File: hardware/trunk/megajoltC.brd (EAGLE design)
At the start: 79.9 x 63 mm, 92 parts, among them IC2 MCP1826, IC9 74AC240, U3 MAX9924, U4 ZXMS6004FF, U5 MAX9924, U6 ZXMS6004FF, U7 MCP1700, U8 FAN8303, X1 MINI_USB_SHIELD, X2 MOLEX_MINIFIT-22

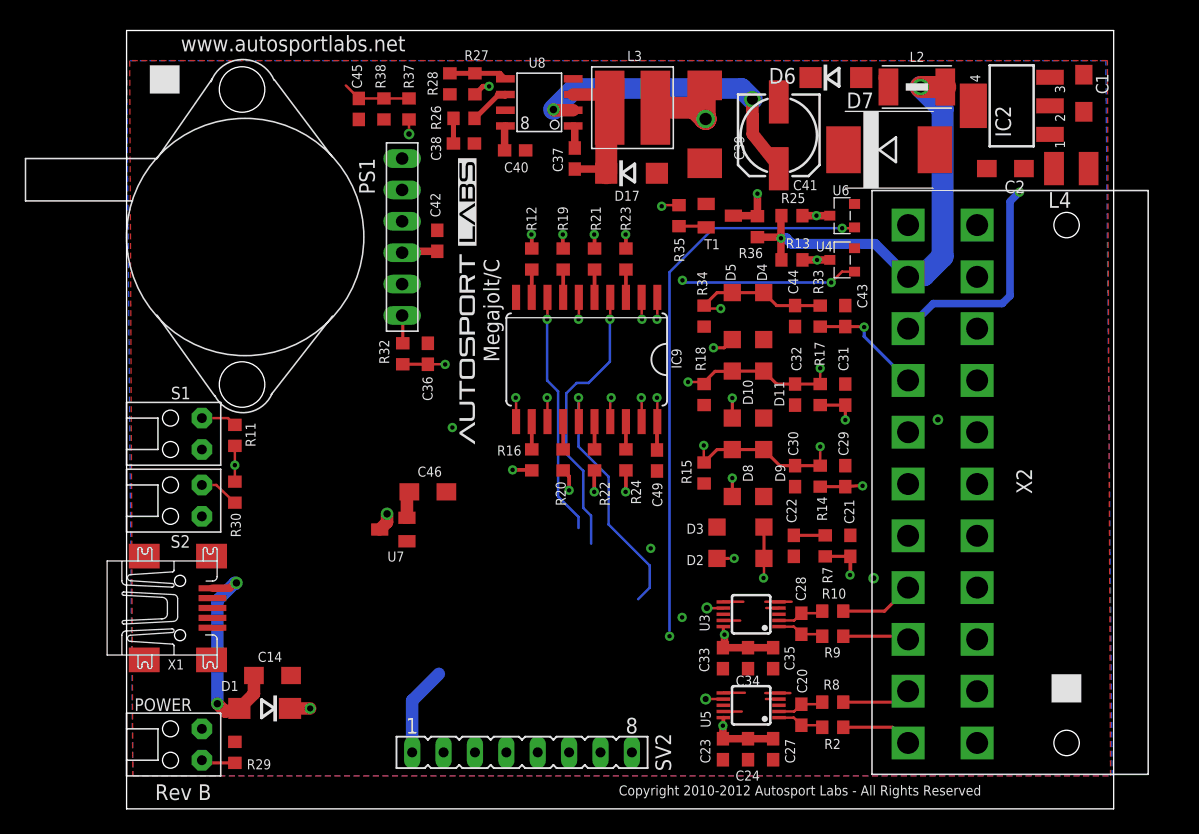
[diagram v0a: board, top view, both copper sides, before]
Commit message: Schematic V1 for MJ2/C
Also added pinmux for xmc4200.  Board is partially routed to assist in pinout
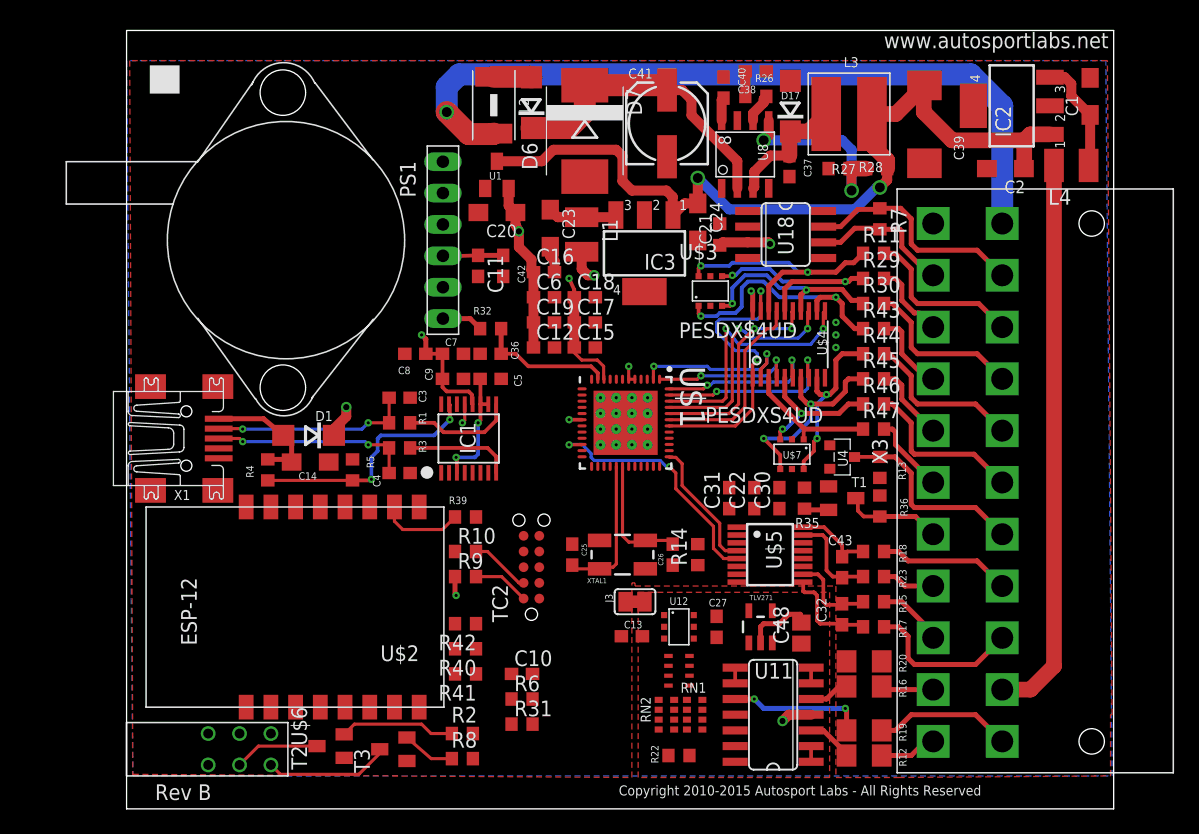
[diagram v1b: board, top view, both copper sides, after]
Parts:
- removed C28: 1nF, rcl:C0603
- removed C29: .001uf, rcl:C0603
- removed C33: 10nF, rcl:C0603
- removed C34: 0.1uF, rcl:C0603
- removed C35: 1uF, rcl:C0603
- removed C44: 0.22uf, rcl:C0603
- removed C45: .1uf, rcl:C0603
- removed C46: 10uF, rcl:SMC_A
- removed C49: 0.1uf, rcl:C0603
- removed D10, D11, D2, D3, D4, D5, D8, D9: schottky, smt_diodes:SOD123
- removed IC9: 74AC240, 74xx-eu:SO20W
- removed POWER, S1, S2: PANEL_LED, LEDs:RIGHTANGLE_CML_5323F5
- removed R21, R24, R25: 1K, rcl:R0603
- removed R33: 20K 1%, rcl:R0603
- removed R34: 39K 1%, rcl:R0603
- removed R37: 51K 1%, rcl:R0603
- removed R38: 10K 1%, rcl:R0603
- removed SV2: (no value), con-lsta:FE08
- removed U3, U5: MAX9924, max9924_9927:UMAX10
- removed U6: ZXMS6004FF, power_mosfets:SOT-23
- removed U7: MCP1700, mcp1700:SOT-23
- removed X2: MOLEX_MINIFIT-22, molex_mini-fit:MOLEX_MINIFIT-22
- added C10, C12: 10uF, resistor:C0603
- added C11: 0.1uf, rcl:C0603
- added C13, C15, C16, C17, C18, C19, C7, C8: 100nF, resistor:C0603
- added C25, C26: 33pF, SparkFun:0603
- added C3, C4: 47pF, resistor:C0603
- added C48: 0.1uF, rcl:C0805
- added C5: 100nf, resistor:C0603
- added C6, C9: 4.7uF, resistor:C0603
- added CN2: (no value), cap_array:1206_ARRAY
- added IC1: IC_FT230X-SSOP-16, dp_devices:SSOP-16-FTDI
- added IC3: MCP1826, linear:SOT223
- added J3: JUMPER_CLOSEDTHICK, jumpers:JUMPER_CLOSED_THICK
- added L1: 1uH, smt_inductors:1210
- added R1, R3: 27, resistor:R0603
- added R31: 100, resistor:R0603
- added R39: 1k, resistor:R0603
- added R4: 4.7k, resistor:R0603
- added R40, R41, R42: 100, rcl:R0603
- added R43, R44, R45, R46, R47: 1K, rcl:R0603
- added R5, R6: 10k, resistor:R0603
- added RN1: 5.6K, resistor-dil:0603-ARC
- added RN2: 10K, resistor-dil:0603-ARC
- added T2, T3: (no value), transistor:SOT23-EBC
- added TC2: TC2050-IDC-NL, TagConnect:TC2050-IDC-NL
- added TLV271: TLV271, texas_instruments:SOT23-5
- added U$1: INF-PG-VQFN-48-53-5200X5200TE5, infineon_xmc:INF-PG-VQFN-48-53-5200X5200TE5PRIMARY
- added U$2: ESP8266_ESP-12, ESP8266-ESP12:ESP8266-ESP12
- added U$3, U$7, U12: PESDXS4UD, smt_diodes:SC-74
- added U$4: 74AC240, dp_devices:TSSOP-20
- added U$5: MAX9926, max9924_9927:QSOP16
- added U$6: TRIPLE_PANEL_LED, LEDs:RIGHT_ANGLE_3_LEDS_DEEP
- added U1: MCP1700, mcp1700:SOT-23
- added U11: TLV274, op_amps:SO14
- added U18: MCP2551SO8, can:SO08
- added X3: MOLEX_MINIFIT-22, molex_mini-fit:MOLEX_MINIFIT-22
- added XTAL1: 8MHz, SparkFun2:CRYSTAL-SMD-5X3
- C20: value 1nF -> 10uF; device rcl:C0603 -> rcl:SMC_A
- C21: value .001uF -> 0.1uF; device rcl:C0603 -> rcl:C0603K
- C22: value 0.22uF -> 10nF
- C23: value 10nF -> 10uF; device rcl:C0603 -> rcl:SMC_A
- C24: value 0.1uF -> 10uF; device rcl:C0603 -> rcl:SMC_A
- C27: value 1uF -> .1uf; device rcl:C0603 -> resistor:C0603
- C30: value 0.22uf -> 0.1uF
- C31: value .001uf -> 1uF
- C32: value 0.22uf -> 1nF
- C43: value .001uf -> 1nF
- R10, R9: value 10K -> 100k; device rcl:R0603 -> resistor:R0603
- R11, R29, R30: value 100 -> 1K
- R12, R16, R19, R20: value 1K -> 10K; device rcl:R0603 -> rcl:R1206
- R14, R17: value 20K 1% -> 10K
- R15, R18: value 39K 1% -> 10K
- R22: value 1K -> 2.1k; device rcl:R0603 -> resistor:R0603
- R23: value 1K -> 10K
- R27: value 18K 1% -> 24K 1%
- R28: value 2.43K 1% -> 2.94K 1%
- R7: value 2.2K -> 120
- moved R29 64.4 mm to (60.5, 42.9), turned to 0 degrees
- moved R30 53.9 mm to (60.5, 40.9), turned to 0 degrees
- moved R11 53.7 mm to (60.5, 45.0), turned to 0 degrees
- moved R12 48.3 mm to (59.7, 4.32), turned to 0 degrees
- moved C20 47.5 mm to (30.0, 48.3), turned to 180 degrees
- moved R19 45.3 mm to (59.7, 6.35), turned to 0 degrees
- moved C23 44.4 mm to (34.3, 47.0)
- moved C24 42.9 mm to (46.2, 47.5)
- moved L2 34.3 mm to (29.7, 56.9), turned to 270 degrees
- moved R27 33.2 mm to (60.7, 51.8), turned to 180 degrees
- moved R23 32.6 mm to (60.5, 18.8), turned to 0 degrees
- moved R16 32.6 mm to (59.7, 9.91), turned to 0 degrees
- moved R28 32.2 mm to (57.7, 51.8), turned to 180 degrees
- moved R8 30.3 mm to (27.2, 4.06)
- moved R10 30.1 mm to (27.4, 20.8)
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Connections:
- removed net +12V: L2.2, R13.2, R25.2, R36.2, X2.P2
- removed net +6V: C2.+, IC2.1
- removed net ADC0: C45.1, R37.2, R38.1
- removed net ADC4: C30.1, D8.A, D9.C, R14.2, R15.2
- removed net ADC5: C32.1, D10.A, D11.C, R17.2, R18.2
- removed net ADC6: C36.1, R32.2
- removed net ADC7: C44.1, D4.C, D5.A, R33.2, R34.2
- removed net AUX_IN: C29.1, R14.1, X2.P6
- removed net GPI0: D2.A, D3.C
- removed net GPO0: IC9.11
- removed net GPO1: IC9.8
- removed net GPO10: IC9.1, IC9.19
- removed net GPO11: U4.1
- removed net GPO2: IC9.13
- removed net GPO3: IC9.6
- removed net GPO4: IC9.15
- removed net GPO5: IC9.4
- removed net GPO6: IC9.17
- removed net GPO7: IC9.2
- removed net GPO8: R35.1
- removed net GPO9: U6.1
- removed net N$14: C20.2, R8.1, U5.2
- removed net N$19: R11.2, S1.A
- removed net N$6: C28.2, R10.1, U3.2
- removed net OPTION_IN: C21.1, R7.1, X2.P7
- removed net PROC_PULSE_IN: C22.1, R7.2
- removed net RESET: SV2.2
- removed net SAFE12V: C41.+, D6.C, D7.C, R37.1, U8.2
- removed net SHIFT_LIGHT: R25.1, U6.3, X2.P20
- removed net TCK: SV2.5
- removed net TDI: SV2.3
- removed net TDO: SV2.6
- removed net TEMP_IN: C43.1, R33.1, X2.P4
- removed net TIMER0: U5.7
- removed net TIMER1: U3.7
- removed net TMS: SV2.4
- removed net V+: C46.+, SV2.1, U7.2
- new net +3V3: C12.1, C13.1, C15.1, C16.1, C17.1, C18.1, C19.1, C20.+, C6.1, C7.1, C8.1, C9.1, IC1.12, R31.2, R6.2, R9.1, TC2.1, U$1.10, U$1.18, U$1.28, U$1.31, U$1.41, U$1.5, U$1.6, U$2.16, U1.2
- new net AGND: C13.2, C27.2, C48.2, CN2.1, CN2.2, CN2.4, J3.1, R22.1, RN2.1, RN2.2, RN2.3, TLV271.2, U$1.17, U11.11, U12.2, U12.5
- new net ANALOG-FREQ_1_OPAMP_OUT1: RN1.6, U11.1, U11.2
- new net ANALOG-FREQ_1_OPAMP_OUT2: RN1.7, U11.6, U11.7
- new net ANALOG-FREQ_1_OPAMP_OUT3: RN1.8, U11.8, U11.9
- new net ANALOG-FREQ_1_OPAMP_OUT4: RN1.4, TLV271.1, TLV271.4
- new net CAM_TIM_IN: U$1.22, U$5.5
- new net CANH: R7.1, U18.7, X3.P21
- new net CANL: R7.2, U18.6, X3.P2
- new net CAN_RX: U$1.15, U18.4
- new net CAN_TX: U$1.26, U18.1
- new net CLT_ADC: RN1.3, RN2.6, U$1.16
- new net CLT_IN: R12.2, X3.P11
- new net CRANK_TIM_IN: U$1.37, U$5.4
- new net ESP_GPIO0: U$2.4
- new net ESP_RXD: U$1.21, U$2.7
- new net ESP_TXD: U$1.24, U$2.8
- new net FTDI_DM: C3.1, R1.1, X1.2
- new net FTDI_DP: C4.1, R3.1, X1.3
- new net FTDI_RXD: IC1.4, U$1.35
- new net FTDI_TXD: IC1.1, U$1.36
- new net FTDI_VBUS_SENSE: IC1.15, R4.1, R5.2
- new net GPO_COIL1: U$1.2, U$4.2
- new net GPO_COIL2: U$1.1, U$4.4
- new net GPO_COIL3: U$1.48, U$4.6
- new net GPO_COIL4: U$1.47, U$4.8
- new net GPO_COIL5: U$1.46, U$4.11
- new net GPO_COIL6: U$1.45, U$4.13
- new net GPO_COIL7: U$1.44, U$4.15
- new net GPO_COIL8: U$1.43, U$4.17
- new net GPO_COIL_EN: U$1.42, U$4.1, U$4.19
- new net IAT_ADC: RN1.1, RN2.8, U$1.14
- new net IAT_IN: R19.2, X3.P12
- new net MAP_ADC: C36.1, R32.2, U$1.11
- new net MAX_DIRN: R14.1, U$5.12
- new net N$1: IC1.8, R3.2
- new net N$17: C10.1, R6.1, U$2.9
- new net N$18: R31.1, U$2.11
- new net N$20: R40.2, U$6.1
- new net N$23: R42.2, U$6.5
- new net N$24: R39.2, U$2.2
- new net N$25: C25.2, U$1.29, XTAL1.3
- new net N$36: R11.1, U$3.6, U$4.18
- new net N$37: R29.1, U$3.4, U$4.16
- new net N$38: R30.1, U$3.3, U$4.14
- new net N$39: R43.1, U$3.1, U$4.12
- new net N$4: C5.1, IC1.10, IC1.11, IC1.3
- new net N$40: R44.1, U$4.9, U$7.6
- new net N$41: R45.1, U$4.7, U$7.4
- new net N$42: R46.1, U$4.5, U$7.3
- new net N$43: R47.1, U$4.3, U$7.1
- new net N$56: C23.+, IC3.3, L1.1
- new net PGM_GPO: U$1.23, U4.1
- new net RAW_+12V: L2.2, X3.P22
- new net SAFE_+12V: C27.1, C41.+, D6.C, D7.C, R13.2, R20.2, R36.2, TLV271.5, U8.2
- new net STATUS_LED_1: R2.2, U$1.20
- new net STATUS_LED_2: R8.2, U$1.19
- new net SWCLK: R10.2, TC2.4, U$1.34
- new net SWDIO: R9.2, TC2.2, U$1.33
- new net TACH_GPO: R35.1, U$1.25
- new net TPS_ADC: RN1.2, RN2.7, U$1.13
- new net VBATT_ADC: R22.2, RN1.5, U$1.12
- new net VDD: C2.+, C24.+, C39.+, IC2.1, IC3.1, L3.P$1, R27.1, U1.3
- new net XMC_RESET: TC2.10, U$1.32
- net +5V: now also C11.1, C21.1, C22.1, C30.1, C31.1, L1.2, R14.2, R40.1, R41.1, R42.1, U$4.20, U$5.14, U11.4, U18.3; no longer C23.1, C24.1, C27.1, C33.1, C34.1, C35.1, C39.+, C49.1, D10.C, D2.C, D5.C, D8.C, IC9.20, L3.P$1, R11.1, R27.1, R30.1, U3.10, U5.10, U7.3
- net CAM_VRS+: now also R17.2, X3.P14; no longer R9.2, X2.P9
- net CAM_VRS-: now also R15.2, X3.P9; no longer R10.2, X2.P8
- net COIL1: now also R11.2, X3.P20; no longer R12.2, X2.P12
- net COIL2: now also R29.2, X3.P3; no longer R16.2, X2.P13
- net COIL3: now also R30.2, X3.P19; no longer R19.2, X2.P14
- net COIL4: now also R43.2, X3.P4; no longer R20.2, X2.P15
- net COIL5: now also R44.2, X3.P18; no longer R21.2, X2.P16
- net COIL6: now also R45.2, X3.P5; no longer R22.2, X2.P17
- net COIL7: now also R46.2, X3.P17; no longer R23.2, X2.P18
- net COIL8: now also R47.2, X3.P6; no longer R24.2, X2.P19
- net CRANK_VRS+: now also R18.2, X3.P15; no longer R2.2, X2.P11
- net CRANK_VRS-: now also R23.2, X3.P8; no longer R8.2, X2.P10
- net GND: now also C10.2, C11.2, C12.2, C15.2, C16.2, C17.2, C18.2, C19.2, C20.-, C23.-, C24.-, C25.1, C26.1, C3.2, C4.2, C5.2, C6.2, C7.2, C8.2, C9.2, IC1.13, IC1.5, IC3.2, IC3.4, J3.2, R10.1, R39.1, R5.1, T2.E, T3.E, TC2.3, U$1.27, U$1.49, U$2.1, U$3.2, U$3.5, U$4.10, U$5.1, U$5.11, U$5.13, U$5.3, U$5.6, U$5.8, U$6.2, U$7.2, U$7.5, U1.1, U18.2, U18.8, X3.P1; no longer C23.2, C24.2, C27.2, C29.2, C32.2, C33.2, C34.2, C35.2, C43.2, C44.2, C45.2, C46.-, C49.2, D11.A, D3.A, D4.A, D9.A, IC9.10, R15.1, R18.1, R29.2, R34.1, R38.2, SV2.7, SV2.8, U3.4, U3.5, U3.6, U3.9, U5.4, U5.5, U5.6, U5.9, U6.2, U7.1, X2.P1
- net N$2: now also T2.B; no longer C20.1, U5.1
- net N$21: now also C26.2, U$1.30, XTAL1.1; no longer R30.2, S2.A
- net N$22: now also R41.2, U$6.3; no longer POWER.C, R29.1
- net N$26: now also CN2.7, U11.3, U12.1; no longer IC9.9
- net N$27: now also C43.1, R18.1, U$5.16; no longer IC9.12, R16.1
- net N$28: now also CN2.8, R16.1, U11.5, U12.6; no longer IC9.7, R19.1
- net N$29: now also C32.1, R15.1, U$5.10; no longer IC9.14, R20.1
- net N$3: now also IC1.9, R1.2; no longer X1.3
- net N$30: now also CN2.5, R19.1, U11.10, U12.4; no longer IC9.5, R21.1
- net N$31: now also C48.1, R20.1, TLV271.3, U12.3; no longer IC9.16, R22.1
- net N$32: now also C32.2, R17.1, U$5.9; no longer IC9.3, R23.1
- net N$33: now also C43.2, R23.1, U$5.15; no longer IC9.18, R24.1
- net N$5: now also R8.1, T3.B; no longer C28.1, R9.1, U3.1
- net PGM_OUT: now also X3.P16; no longer X2.P21
- net PROC_STATUS_LED_OUT1: now also T2.C, U$6.4; no longer S1.C
- net PROC_STATUS_LED_OUT2: now also T3.C, U$6.6; no longer S2.C
- net TACH_OUT: now also X3.P7; no longer X2.P22
- net TPS_IN: now also R16.2, X3.P10; no longer C31.1, R17.1, X2.P5
- net VBUS: now also R4.2
- net VREF: now also X3.P13; no longer X2.P3
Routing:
- net VDD: track 0.00 -> 67.6 mm, vias 0 -> 2
- net COIL1: track 78.4 -> 13.4 mm, vias 1 -> 0
- net RAW_+12V: track 0.00 -> 62.5 mm, vias 0 -> 1
- net COIL3: track 68.4 -> 13.3 mm, vias 1 -> 0
- net TDI: track 49.1 -> 0.00 mm
- net COIL2: track 54.8 -> 6.35 mm, vias 3 -> 0
- net GPO9: track 48.4 -> 0.00 mm, vias 2 -> 0
- net ADC7: track 41.3 -> 0.00 mm, vias 1 -> 0
- net GPO11: track 41.0 -> 0.00 mm, vias 2 -> 0
- net SAFE12V: track 38.7 -> 0.00 mm, vias 3 -> 0
- net GPO8: track 38.5 -> 0.00 mm, vias 1 -> 0
- net ADC5: track 38.0 -> 0.00 mm, vias 3 -> 0
- net +12V: track 37.8 -> 0.00 mm, vias 2 -> 0
- net GPO10: track 37.8 -> 0.00 mm, vias 2 -> 0
- net +3V3: track 0.00 -> 36.9 mm, vias 0 -> 6
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- added copper zone on layer 15, net +3V3
- added copper zone on layer 1, net AGND
- added copper zone on layer 2, net GND
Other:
- board text added: "Copyright 2010-2015 Autosport Labs - All Rights Reserved"
- board text removed: "Copyright 2010-2012 Autosport Labs - All Rights Reserved"

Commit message: Schematic, second draft complete
Also added gitignore
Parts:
- removed C27: .1uf, resistor:C0603
- removed C48: 0.1uF, rcl:C0805
- removed L4: 1uH, smt_inductors:1210
- removed R20: 10K, rcl:R1206
- removed R22: 2.1k, resistor:R0603
- removed T2, T3: (no value), transistor:SOT23-EBC
- removed TLV271: TLV271, texas_instruments:SOT23-5
- removed X3: MOLEX_MINIFIT-22, molex_mini-fit:MOLEX_MINIFIT-22
- added C28: .1uf, resistor:C0603
- added C45: .1uf, rcl:C0603
- added D2: (no value), diode:SMC
- added D4: PESD1CAN, diode:SOT23
- added R21, R24: 10k, resistor:R0603
- added R37: 43K 1%, rcl:R0603
- added R38: 10K 1%, rcl:R0603
- added U$8: 24LC64-I/SN, element14_microchip:SOIC127P600X175-8N
- added U$9: XMC4200F64K256QFP64, infineon_xmc:INF-PG-LQFP-64-5800X5800T28
- R2: device rcl:R0603 -> rcl:R1206
- R28: value 2.94K 1% -> 2.7K 1%
- R32: value 270 -> 5.6k
- R8: value 10K -> 10k
- U$1: value INF-PG-VQFN-48-53-5200X5200TE5 -> MOLEX_MINIFIT-JR-24; device infineon_xmc:INF-PG-VQFN-48-53-5200X5200TE5PRIMARY -> molex_mini-fit:MOLEX_MINIFIT-JR-24
- moved C1 50.8 mm to (28.4, 46.5), turned to 270 degrees
- moved IC2 40.8 mm to (32.8, 44.5), turned to 180 degrees
- moved R8 36.6 mm to (29.2, 40.6)
- moved C2 34.6 mm to (37.1, 45.5), turned to 270 degrees
- moved R2 33.0 mm to (59.7, 11.9)
- moved U$1 32.8 mm to (73.2, 30.5)
- moved U1 31.5 mm to (61.0, 57.1)
- moved C20 31.5 mm to (61.2, 52.3), turned to 270 degrees
- moved L1 31.4 mm to (65.8, 58.7), turned to 0 degrees
- moved C12 16.1 mm to (29.5, 21.8)
- moved C15 16.1 mm to (32.8, 21.8)
- moved C18 16.1 mm to (32.8, 25.9)
- moved C6 16.1 mm to (29.5, 25.9)
- moved C17 16.1 mm to (32.8, 23.9)
- moved C16 16.1 mm to (29.5, 27.9)
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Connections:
- removed net ANALOG-FREQ_1_OPAMP_OUT4: RN1.4, TLV271.1, TLV271.4
- removed net N$5: R8.1, T3.B
- removed net N$53: C1.+, IC2.3, L4.1
- removed net N$56: C23.+, IC3.3, L1.1
- removed net PROC_STATUS_LED_OUT1: T2.C, U$6.4
- removed net PROC_STATUS_LED_OUT2: T3.C, U$6.6
- new net AUX_ADC: RN1.4, RN2.5, U$9.19
- new net AUX_IN: R2.2, U$1.P14
- new net EEPROM_SCL: R24.1, U$8.6, U$9.59
- new net EEPROM_SDA: R21.1, U$8.5, U$9.62
- new net N$14: RN1.5, U11.13, U11.14
- new net UNUSED: U$1.P10
- new net VCC: C1.+, IC2.3, R31.2, R6.2, U$2.16
- net +3V3: now also C28.1, R21.2, R24.2, R40.1, R41.1, R42.1, U$8.8, U$9.13, U$9.22, U$9.38, U$9.42, U$9.56, U$9.8, U$9.9; no longer R31.2, R6.2, U$1.10, U$1.18, U$1.28, U$1.31, U$1.41, U$1.5, U$1.6, U$2.16
- net +5V: now also C23.+, IC3.3, L1.1; no longer L1.2, R40.1, R41.1, R42.1
- net AGND: now also C45.2, CN2.6, R38.2, RN2.4, U$9.21; no longer C27.2, C48.2, R22.1, TLV271.2, U$1.17
- net CAM_TIM_IN: now also U$9.30; no longer U$1.22
- net CAM_VRS+: now also U$1.P16; no longer X3.P14
- net CAM_VRS-: now also U$1.P9; no longer X3.P9
- net CANH: now also D4.2, U$1.P23; no longer X3.P21
- net CANL: now also D4.1, U$1.P2; no longer X3.P2
- net CAN_RX: now also U$9.36; no longer U$1.15
- net CAN_TX: now also U$9.34, U$9.35; no longer U$1.26
- net CLT_ADC: now also U$9.20; no longer U$1.16
- net CLT_IN: now also U$1.P12; no longer X3.P11
- net COIL1: now also U$1.P22; no longer X3.P20
- net COIL2: now also U$1.P3; no longer X3.P3
- net COIL3: now also U$1.P21; no longer X3.P19
- net COIL4: now also U$1.P4; no longer X3.P4
- net COIL5: now also U$1.P20; no longer X3.P18
- net COIL6: now also U$1.P5; no longer X3.P5
- net COIL7: now also U$1.P19; no longer X3.P17
- net COIL8: now also U$1.P6; no longer X3.P6
- net CRANK_TIM_IN: now also U$9.28; no longer U$1.37
- net CRANK_VRS+: now also U$1.P17; no longer X3.P15
- net CRANK_VRS-: now also U$1.P8; no longer X3.P8
- net ESP_GPIO0: now also U$9.49
- net ESP_RXD: now also U$9.29; no longer U$1.21
- net ESP_TXD: now also U$9.32; no longer U$1.24
- net FTDI_RXD: now also U$9.47; no longer U$1.35
- net FTDI_TXD: now also U$9.48; no longer U$1.36
- net GND: now also C28.2, D4.3, R8.1, U$1.P1, U$8.1, U$8.2, U$8.3, U$8.4, U$9.37, U$9.41, U$9.65; no longer T2.E, T3.E, U$1.27, U$1.49, X3.P1
- net GPO_COIL1: now also U$9.2; no longer U$1.2
- net GPO_COIL2: now also U$9.1; no longer U$1.1
- net GPO_COIL3: now also U$9.64; no longer U$1.48
- net GPO_COIL4: now also U$9.63; no longer U$1.47
- net GPO_COIL5: now also U$9.61; no longer U$1.46
- net GPO_COIL6: now also U$9.60; no longer U$1.45
- net GPO_COIL7: now also U$9.58; no longer U$1.44
- net GPO_COIL8: now also U$9.57; no longer U$1.43
- net GPO_COIL_EN: now also U$9.4; no longer U$1.42
- net IAT_ADC: now also U$9.18; no longer U$1.14
- net IAT_IN: now also U$1.P13; no longer X3.P12
- net MAP_ADC: now also R8.2, U$9.15; no longer U$1.11
- net N$2: now also D2.A, L1.2; no longer R2.1, T2.B
- net N$21: now also U$9.40; no longer U$1.30
- net N$25: now also U$9.39; no longer U$1.29
- net N$31: now also CN2.3, R2.1, U11.12; no longer C48.1, R20.1, TLV271.3
- net PGM_GPO: now also U$9.31; no longer U$1.23
- net PGM_OUT: now also U$1.P18; no longer X3.P16
- net RAW_+12V: now also U$1.P24; no longer X3.P22
- net SAFE_+12V: now also R37.1; no longer C27.1, R20.2, TLV271.5
- net STATUS_LED_1: now also U$6.4, U$9.27; no longer R2.2, U$1.20
- net STATUS_LED_2: now also U$6.6, U$9.26; no longer R8.2, U$1.19
- net SWCLK: now also U$9.45; no longer U$1.34
- net SWDIO: now also U$9.44; no longer U$1.33
- net TACH_GPO: now also U$9.33; no longer U$1.25
- net TACH_OUT: now also U$1.P7; no longer X3.P7
- net TPS_ADC: now also U$9.17; no longer U$1.13
- net TPS_IN: now also U$1.P11; no longer X3.P10
- net VBATT_ADC: now also C45.1, R37.2, R38.1, U$9.16; no longer R22.2, RN1.5, U$1.12
- net VREF: now also D2.C, U$1.P15; no longer L4.2, X3.P13
- net XMC_RESET: now also U$9.43; no longer U$1.32
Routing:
- net RAW_+12V: track 62.5 -> 0.00 mm, vias 1 -> 0
- net VDD: track 67.6 -> 37.6 mm, vias 2 -> 0
- net GPO_COIL_EN: track 24.2 -> 0.00 mm, vias 2 -> 0
- net SAFE_+12V: track 24.9 -> 1.42 mm
- net +3V3: track 36.9 -> 15.5 mm, vias 6 -> 0
- net GPO_COIL5: track 20.9 -> 0.00 mm, vias 2 -> 0
- net CAM_TIM_IN: track 20.4 -> 0.00 mm, vias 2 -> 0
- net GPO_COIL4: track 15.2 -> 0.00 mm, vias 2 -> 0
- net N$8: track 15.7 -> 1.35 mm, vias 2 -> 0
- net FTDI_DP: track 16.1 -> 2.03 mm, vias 2 -> 0
- net GPO_COIL1: track 13.4 -> 0.00 mm, vias 2 -> 0
- net FTDI_VBUS_SENSE: track 19.7 -> 6.86 mm, vias 2 -> 0
- net FTDI_DM: track 16.0 -> 3.99 mm, vias 2 -> 0
- net GPO_COIL2: track 11.8 -> 0.00 mm, vias 2 -> 0
- net GPO_COIL8: track 15.7 -> 4.57 mm
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
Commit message: Board routed. V1
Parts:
- D2: value (none) -> SCHOTTKY; device diode:SMC -> smt_diodes:SMA
- moved L1 9.18 mm to (74.9, 57.9), turned to 90 degrees
- moved D2 4.01 mm to (77.7, 57.4), turned to 90 degrees
- moved R38 1.14 mm to (49.5, 14.5), turned to 90 degrees
- moved CN2 0.76 mm to (44.7, 11.9)
- moved R8 0.76 mm to (29.2, 41.4)
- moved C36 0.57 mm to (29.2, 37.3)
- moved C23 0.51 mm to (35.8, 49.8)
- moved C37 0.51 mm to (47.0, 52.5)
- moved U12 0.51 mm to (44.7, 15.2)
- moved C24 0.51 mm to (45.7, 47.0)
- moved R32 0.51 mm to (29.2, 39.4)
- moved C7 0.25 mm to (25.1, 37.1)
- moved C8 0.25 mm to (22.1, 37.1)
- moved TC2 0.25 mm to (34.0, 17.0)
- moved C5 0.25 mm to (28.2, 35.1)
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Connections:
- new net ESP_GPIO2: U$2.3, U$9.49
- net CAN_TX: no longer U$9.34
- net ESP_GPIO0: now also U$9.50; no longer U$9.49
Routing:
- net VCC: track 2.52 -> 120.9 mm, vias 0 -> 2
- net SAFE_+12V: track 1.42 -> 91.5 mm, vias 0 -> 3
- net RAW_+12V: track 0.00 -> 68.5 mm, vias 0 -> 1
- net +3V3: track 15.5 -> 79.4 mm, vias 0 -> 12
- net ESP_GPIO0: track 0.00 -> 57.3 mm, vias 0 -> 2
- net ESP_GPIO2: track 0.00 -> 55.5 mm, vias 0 -> 2
- net STATUS_LED_1: track 0.00 -> 53.1 mm, vias 0 -> 1
- net STATUS_LED_2: track 0.00 -> 50.1 mm, vias 0 -> 1
- net VBATT_ADC: track 0.00 -> 42.8 mm, vias 0 -> 2
- net AGND: track 0.00 -> 42.3 mm, vias 0 -> 2
- net AUX_ADC: track 2.05 -> 43.5 mm, vias 0 -> 2
- net GPO_COIL_EN: track 0.00 -> 41.0 mm, vias 0 -> 3
- net EEPROM_SDA: track 2.17 -> 41.0 mm, vias 0 -> 2
- net N$31: track 0.00 -> 37.3 mm, vias 0 -> 5
- net SWCLK: track 0.00 -> 37.1 mm, vias 0 -> 3
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- added copper zone on layer 1, net N$10
- added copper zone on layer 1, net SAFE_+12V
